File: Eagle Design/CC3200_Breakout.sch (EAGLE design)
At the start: 50 parts, among them J22 M10X2, J23 M10X2, U15 AT25FS010, Y2 32.768KHz, Y3 407MHz

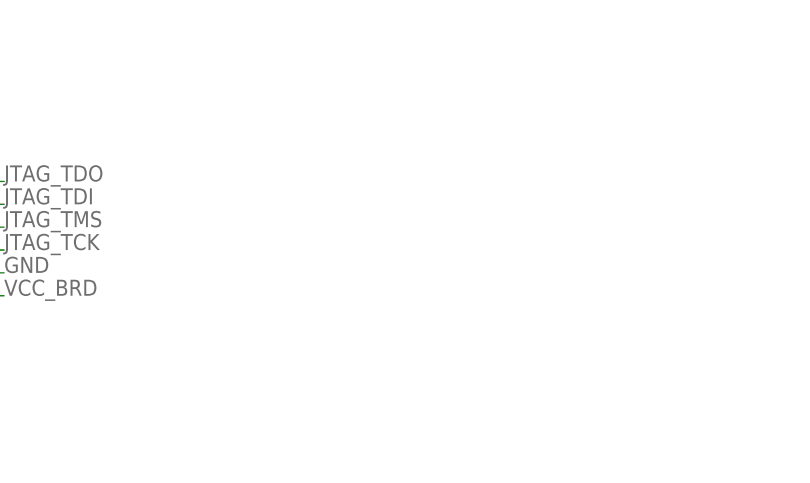
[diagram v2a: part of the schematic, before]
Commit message: Routing
Add connector for Battery JP91
Start Routing
Added design rule for and Gerber of smart-prototyping.
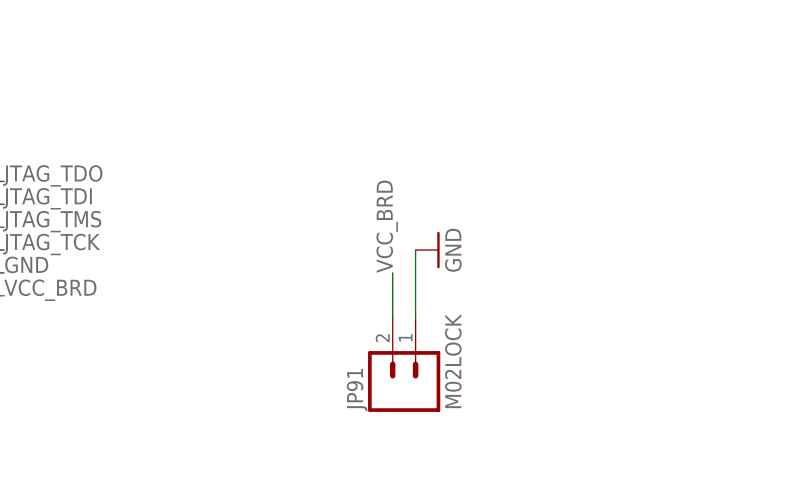
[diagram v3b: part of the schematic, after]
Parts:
- added JP91: M02LOCK, SparkFun-Connectors:M02LOCK
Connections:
- net GND: now also JP91.1
- net VCC_BRD: now also JP91.2
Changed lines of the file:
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@@
 <part name="R61" library="resistor" deviceset="R-US_" device="R0402" value="1k"/>
 <part name="GND25" library="SparkFun-Aesthetics" deviceset="GND" device=""/>
+<part name="JP91" library="SparkFun-Connectors" deviceset="M02" device="LOCK"/>
+<part name="GND30" library="SparkFun-Aesthetics" deviceset="GND" device=""/>
 </parts>
 <sheets>
@@
 <instance part="R61" gate="G$1" x="86.36" y="30.48" rot="R90"/>
 <instance part="GND25" gate="1" x="78.74" y="12.7"/>
+<instance part="JP91" gate="G$1" x="248.92" y="10.16" rot="R90"/>
+<instance part="GND30" gate="1" x="251.46" y="25.4" rot="R90"/>
 </instances>
 <busses>
@@
 <wire x1="78.74" y1="20.32" x2="78.74" y2="15.24" width="0.1524" layer="91"/>
 <pinref part="GND25" gate="1" pin="GND"/>
+</segment>
+<segment>
+<pinref part="JP91" gate="G$1" pin="1"/>
+<wire x1="248.92" y1="17.78" x2="248.92" y2="25.4" width="0.1524" layer="91"/>
+<pinref part="GND30" gate="1" pin="GND"/>
 </segment>
 </net>
@@
 <label x="101.6" y="2.54" size="1.778" layer="95"/>
 </segment>
-</net>
+<segment>
+<pinref part="JP91" gate="G$1" pin="2"/>
+<wire x1="246.38" y1="17.78" x2="246.38" y2="22.86" width="0.1524" layer="91"/>
+<label x="246.38" y="22.86" size="1.778" layer="95" rot="R90"/>
+</segment>
+</net>

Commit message: Routing
Almost finished routing except Anttena
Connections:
- removed net N$34: R65.2
- net 45: now also R65.2
- net VCC_BRD: no longer JP91.2, JTAG.1, R57.1
- net V_BATT: now also JP91.2, JTAG.1, R57.1
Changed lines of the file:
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@@
 <wire x1="157.48" y1="205.74" x2="157.48" y2="210.82" width="0.1524" layer="91"/>
+</segment>
+<segment>
+<pinref part="JP91" gate="G$1" pin="2"/>
+<wire x1="246.38" y1="17.78" x2="246.38" y2="22.86" width="0.1524" layer="91"/>
+<label x="246.38" y="22.86" size="1.778" layer="95" rot="R90"/>
+</segment>
+<segment>
+<pinref part="JTAG" gate="G$1" pin="1"/>
+<wire x1="198.12" y1="20.32" x2="203.2" y2="20.32" width="0.1524" layer="91"/>
+<label x="203.2" y="20.32" size="1.778" layer="95"/>
+</segment>
+<segment>
+<pinref part="R57" gate="G$1" pin="1"/>
+<wire x1="101.6" y1="7.62" x2="101.6" y2="2.54" width="0.1524" layer="91"/>
+<label x="101.6" y="2.54" size="1.778" layer="95"/>
 </segment>
 </net>
@@
 <pinref part="R64" gate="G$1" pin="2"/>
 <pinref part="SUPPLY3" gate="G$1" pin="3.3V"/>
-</segment>
-</net>
-<net name="N$34" class="0">
-<segment>
-<pinref part="R65" gate="G$1" pin="2"/>
-<wire x1="22.86" y1="106.68" x2="17.78" y2="106.68" width="0.1524" layer="91"/>
 </segment>
 </net>
@@
 <label x="193.04" y="142.24" size="1.778" layer="95"/>
 </segment>
-<segment>
-<pinref part="JTAG" gate="G$1" pin="1"/>
-<wire x1="198.12" y1="20.32" x2="203.2" y2="20.32" width="0.1524" layer="91"/>
-<label x="203.2" y="20.32" size="1.778" layer="95"/>
-</segment>
-<segment>
-<pinref part="R57" gate="G$1" pin="1"/>
-<wire x1="101.6" y1="7.62" x2="101.6" y2="2.54" width="0.1524" layer="91"/>
-<label x="101.6" y="2.54" size="1.778" layer="95"/>
-</segment>
-<segment>
-<pinref part="JP91" gate="G$1" pin="2"/>
-<wire x1="246.38" y1="17.78" x2="246.38" y2="22.86" width="0.1524" layer="91"/>
-<label x="246.38" y="22.86" size="1.778" layer="95" rot="R90"/>
-</segment>
 </net>
 <net name="58" class="0">
@@
 <label x="289.56" y="134.62" size="1.778" layer="95"/>
 </segment>
-</net>
+<segment>
+<pinref part="R65" gate="G$1" pin="2"/>
+<wire x1="22.86" y1="106.68" x2="17.78" y2="106.68" width="0.1524" layer="91"/>
+<label x="20.32" y="106.68" size="1.778" layer="95"/>
+</segment>
+</net>

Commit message: Antenna
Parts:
- removed L9: 3.6nH, resistor:L-USL2012C
- added L1: (no value), Spark:INDUCTOR-SPARKFUN0402
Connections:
- net N$36: now also L1.1; no longer L9.1
- net N$37: now also L1.2; no longer L9.2
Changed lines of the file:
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@@
 <layer number="56" name="wert" color="7" fill="1" visible="no" active="no"/>
 <layer number="57" name="tCAD" color="7" fill="1" visible="no" active="no"/>
+<layer number="59" name="tCarbon" color="7" fill="1" visible="no" active="no"/>
+<layer number="60" name="bCarbon" color="7" fill="1" visible="no" active="no"/>
 <layer number="90" name="Modules" color="5" fill="1" visible="yes" active="yes"/>
 <layer number="91" name="Nets" color="2" fill="1" visible="yes" active="yes"/>
@@
 <layer number="127" name="_tValues" color="7" fill="1" visible="yes" active="yes"/>
 <layer number="128" name="_bValues" color="7" fill="1" visible="yes" active="yes"/>
+<layer number="129" name="Mask" color="7" fill="1" visible="yes" active="yes"/>
 <layer number="131" name="tAdjust" color="7" fill="1" visible="yes" active="yes"/>
 <layer number="132" name="bAdjust" color="7" fill="1" visible="yes" active="yes"/>
@@
 <part name="FL1" library="DEA202450" deviceset="DEA202450" device=""/>
 <part name="GND31" library="SparkFun-Aesthetics" deviceset="GND" device=""/>
-<part name="L9" library="resistor" deviceset="L-US" device="L2012C" value="3.6nH"/>
 <part name="GND32" library="SparkFun-Aesthetics" deviceset="GND" device=""/>
 <part name="U$3" library="SparkFun-RF" deviceset="ANTENNA2" device="SMD"/>
@@
 <part name="JP91" library="SparkFun-Connectors" deviceset="M02" device="LOCK"/>
 <part name="GND30" library="SparkFun-Aesthetics" deviceset="GND" device=""/>
+<part name="L1" library="Spark" deviceset="INDUCTOR-SPARKFUN" device="0402"/>
 </parts>
 <sheets>
@@
 <instance part="FL1" gate="G$1" x="231.14" y="208.28"/>
 <instance part="GND31" gate="1" x="231.14" y="190.5"/>
-<instance part="L9" gate="G$1" x="261.62" y="208.28" rot="R90"/>
 <instance part="GND32" gate="1" x="271.78" y="190.5"/>
 <instance part="U$3" gate="G$1" x="284.48" y="213.36"/>
@@
 <instance part="JP91" gate="G$1" x="248.92" y="10.16" rot="R90"/>
 <instance part="GND30" gate="1" x="251.46" y="25.4" rot="R90"/>
+<instance part="L1" gate="G$1" x="261.62" y="208.28" rot="R90"/>
 </instances>
 <busses>
@@
 <segment>
 <pinref part="FL1" gate="G$1" pin="OUT"/>
-<pinref part="L9" gate="G$1" pin="1"/>
 <wire x1="246.38" y1="208.28" x2="254" y2="208.28" width="0.1524" layer="91"/>
+<pinref part="L1" gate="G$1" pin="1"/>
 </segment>
 </net>
 <net name="N$37" class="0">
 <segment>
-<pinref part="L9" gate="G$1" pin="2"/>
 <pinref part="C50" gate="G$1" pin="1"/>
 <wire x1="269.24" y1="208.28" x2="271.78" y2="208.28" width="0.1524" layer="91"/>
@@
 <junction x="271.78" y="208.28"/>
 <pinref part="U$3" gate="G$1" pin="SIGNAL"/>
-</segment>
-</net>
+<pinref part="L1" gate="G$1" pin="2"/>
+</segment>
+</net>

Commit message: Anttena
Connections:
- removed net N$37: C50.1, L1.2, U$3.SIGNAL
- net GND: now also C50.1, L1.2, U$3.SIGNAL
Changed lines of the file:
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@@
 <pinref part="GND30" gate="1" pin="GND"/>
+</segment>
+<segment>
+<pinref part="C50" gate="G$1" pin="1"/>
+<wire x1="269.24" y1="208.28" x2="271.78" y2="208.28" width="0.1524" layer="91"/>
+<wire x1="271.78" y1="208.28" x2="271.78" y2="205.74" width="0.1524" layer="91"/>
+<wire x1="271.78" y1="208.28" x2="284.48" y2="208.28" width="0.1524" layer="91"/>
+<junction x="271.78" y="208.28"/>
+<pinref part="U$3" gate="G$1" pin="SIGNAL"/>
+<pinref part="L1" gate="G$1" pin="2"/>
 </segment>
 </net>
@@
 </segment>
 </net>
-<net name="N$37" class="0">
-<segment>
-<pinref part="C50" gate="G$1" pin="1"/>
-<wire x1="269.24" y1="208.28" x2="271.78" y2="208.28" width="0.1524" layer="91"/>
-<wire x1="271.78" y1="208.28" x2="271.78" y2="205.74" width="0.1524" layer="91"/>
-<wire x1="271.78" y1="208.28" x2="284.48" y2="208.28" width="0.1524" layer="91"/>
-<junction x="271.78" y="208.28"/>
-<pinref part="U$3" gate="G$1" pin="SIGNAL"/>
-<pinref part="L1" gate="G$1" pin="2"/>
-</segment>
-</net>
